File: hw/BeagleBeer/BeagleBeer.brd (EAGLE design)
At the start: 130.8 x 118.7 mm, 104 parts, among them Q10 BSS138, Q9 BSS138, U1 TEMPERATURE-SENSORUMAX8, U4 CAT24C256WI-GT3, U5 BEAGLEBONE_OUTLINEBEAGLEBEER

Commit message: BeagleBeer v2 Run ERCs and DRCs
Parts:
- moved C13 48.2 mm to (71.7, 37.7)
- moved U2 35.9 mm to (66.9, 31.1), turned to 270 degrees
- moved C14 32.0 mm to (62.5, 37.5)
- moved C16 24.2 mm to (61.3, 51.4)
- moved C15 24.1 mm to (71.9, 51.4)
- moved U3 24.0 mm to (66.9, 47.1)
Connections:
- new net N$12: JP2.20, U5.40
- new net N$13: JP2.21, U5.42
- new net N$20: JP1.4, U5.39
- new net N$21: JP1.3, U5.41
- net 3.3V: now also R15.2, R16.2, R22.2, R25.2
- net LED_FLOW_B_3P3: now also U2.3
- net LED_FLOW_C_3P3: no longer JP2.20, U5.40
- net LED_FLOW_D_3P3: no longer JP2.21, U5.42
- net N$2: now also JP1.2, U5.43; no longer R22.2, R25.2
- net N$3: now also JP1.1, U5.45; no longer R15.2, R16.2
- net RELAY_A_3P3: no longer JP1.4, U5.39
- net RELAY_B_3P3: no longer JP1.3, U5.41
- net RELAY_C_3P3: no longer JP1.2, U5.43
- net RELAY_D_3P3: no longer JP1.1, U5.45
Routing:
- net LED_FLOW_D: track 204.4 -> 79.0 mm, vias 12 -> 6
- net LED_FLOW_B: track 159.9 -> 55.1 mm, vias 10 -> 4
- net GPIO_B: track 62.0 -> 125.5 mm
- net GPIO_D: track 90.7 -> 146.5 mm, vias 3 -> 7
- net LED_FLOW_A: track 96.8 -> 50.6 mm, vias 6 -> 4
- net ALARM: track 54.3 -> 94.1 mm, vias 2 -> 5
- net RELAY_D: track 29.5 -> 69.3 mm, vias 2 -> 6
- net LED_FLOW_C: track 133.9 -> 94.6 mm
- net 3.3V: track 304.1 -> 339.9 mm, vias 17 -> 20
- net LED_FLOW_B_3P3: track 6.10 -> 41.8 mm, vias 0 -> 2
- net GPIO_C: track 102.1 -> 137.8 mm, vias 5 -> 7
- net RESET: track 69.3 -> 102.2 mm, vias 2 -> 4
- net ALARM_3P3: track 75.1 -> 43.0 mm
- net RESET_3P3: track 69.4 -> 39.8 mm
- net RELAY_B_3P3: track 71.7 -> 45.2 mm, vias 3 -> 4
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
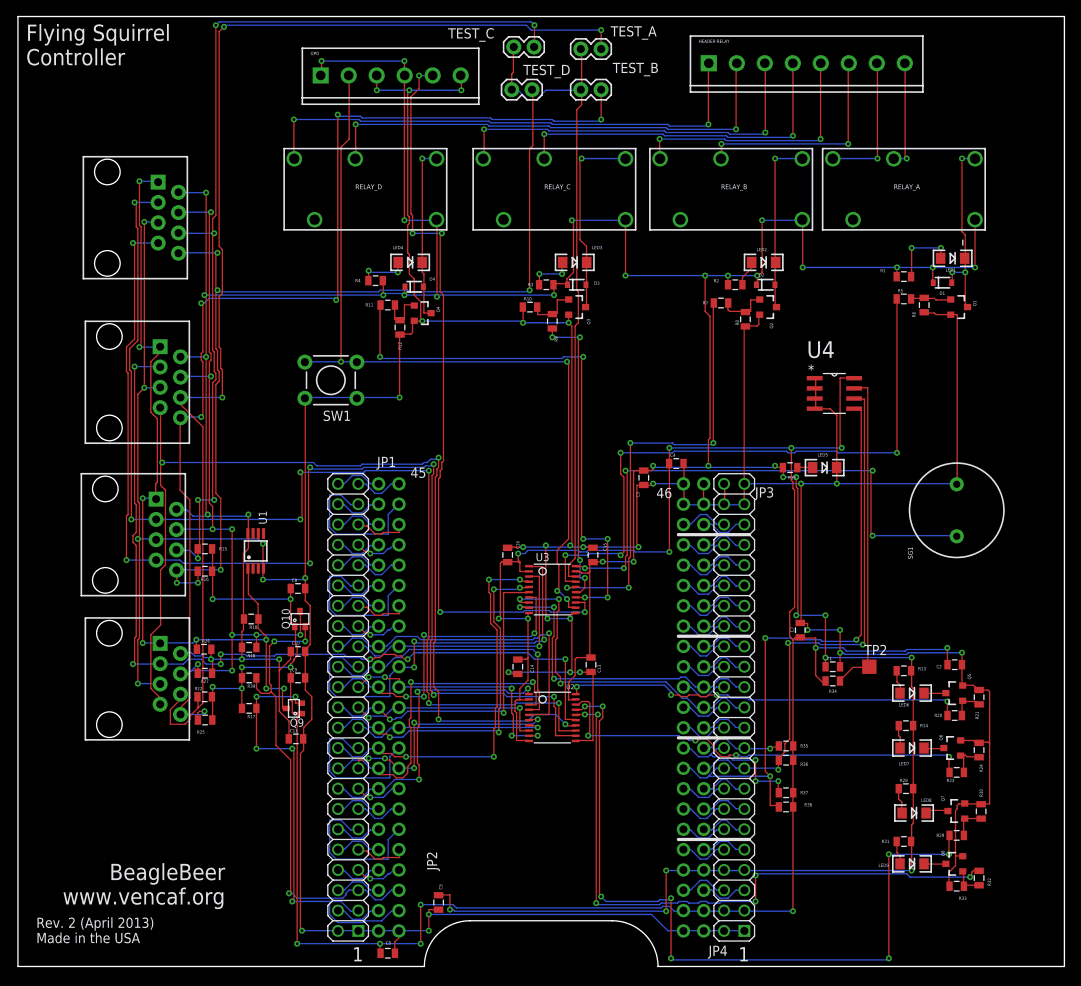
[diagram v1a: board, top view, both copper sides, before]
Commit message: Remove redundant RJ45 connectors on BeagleBeer
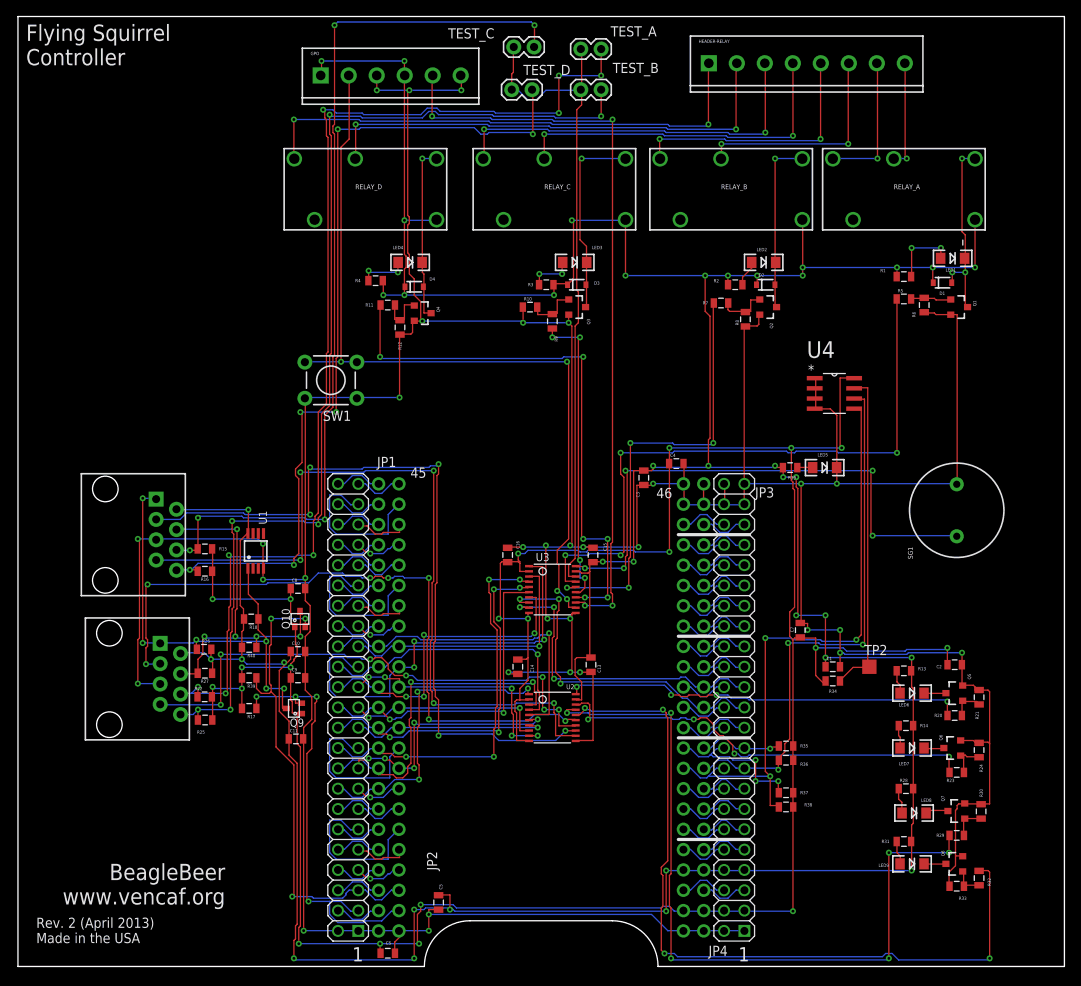
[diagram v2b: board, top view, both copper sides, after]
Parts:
- removed RJ3, RJ4: RJ45-8PTH, SparkFun:RJ45-8
- moved RJ2 19.1 mm to (11.0, 54.0)
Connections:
- net 5V: no longer RJ3.2, RJ4.2
- net FLOW_A: no longer RJ2.6
- net FLOW_B: no longer RJ2.8
- net FLOW_C: now also RJ2.6; no longer RJ3.6, RJ4.6
- net FLOW_D: now also RJ2.8; no longer RJ3.8, RJ4.8
- net GND: no longer RJ3.5, RJ4.5
- net GPIO_A: no longer RJ2.3
- net GPIO_B: no longer RJ2.7
- net GPIO_C: now also RJ2.3; no longer RJ3.3, RJ4.3
- net GPIO_D: now also RJ2.7; no longer RJ3.7, RJ4.7
- net ONEWIRE_A: no longer RJ3.1, RJ4.1
- net ONEWIRE_B: no longer RJ3.4, RJ4.4
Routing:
- net GPIO_B: track 125.5 -> 66.3 mm, vias 4 -> 7
- net ONEWIRE_B: track 94.9 -> 45.2 mm, vias 9 -> 5
- net GPIO_D: track 146.5 -> 97.2 mm, vias 7 -> 5
- net ONEWIRE_A: track 103.8 -> 58.1 mm, vias 8 -> 6
- net GND: track 611.4 -> 567.0 mm, vias 34 -> 32
- net GPIO_C: track 137.8 -> 94.6 mm, vias 7 -> 5
- net 5V: track 508.1 -> 485.8 mm, vias 40 -> 38
- net GPIO_A: track 107.2 -> 85.5 mm
- net LED_FLOW_D: track 79.0 -> 96.6 mm, vias 6 -> 4
- net FLOW_A: track 152.7 -> 136.7 mm, vias 3 -> 8
- net FLOW_D: track 121.3 -> 106.6 mm
- net FLOW_C: track 120.3 -> 113.3 mm, vias 6 -> 5
- net FLOW_B: track 137.8 -> 132.7 mm
- net ONEWIRE_B_3P3: track 57.7 -> 59.9 mm
- net ONEWIRE_A_3P3: track 56.8 -> 54.8 mm, vias 5 -> 4
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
